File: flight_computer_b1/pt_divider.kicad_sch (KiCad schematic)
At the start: 4 parts

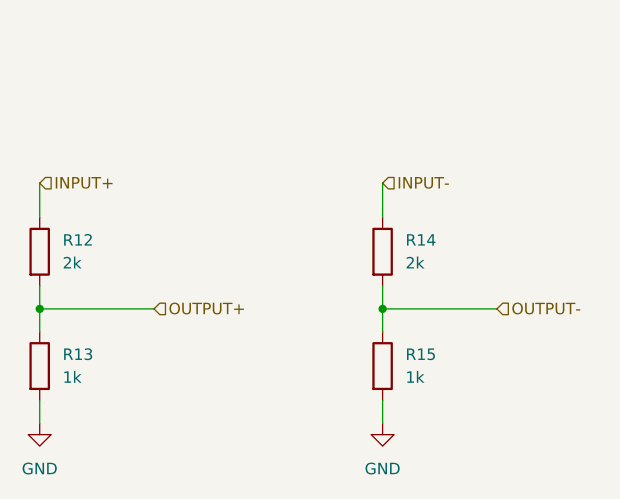
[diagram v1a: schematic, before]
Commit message: flight computer: added mux and voltage sense channels
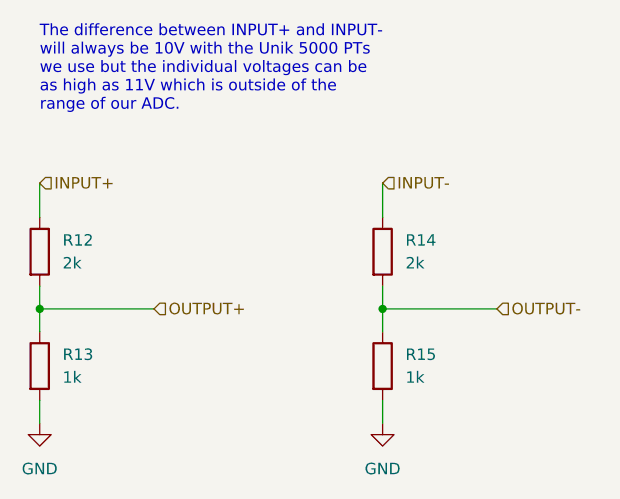
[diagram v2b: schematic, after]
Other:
- note added: "The difference between INPUT+ and INPUT- will always be 10V with the Unik 5000 PTs we use but the individual voltages can be as high as 11V which is outside of the range of our ADC."
- company: (none) -> Purdue Space Program Liquids

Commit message: flight computer: added pyro circuit and digikey part numbers
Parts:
- R12, R14: DIGIKEY PART N (none) -> 749-1706-1-ND
- R13, R15: DIGIKEY PART N (none) -> YAG1237CT-ND
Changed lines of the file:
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@@
+			)
+		)
+		(property "DIGIKEY PART N" "749-1706-1-ND"
+			(at 127 83.82 0)
+			(effects
+				(font
+					(size 1.27 1.27)
+				)
+				(hide yes)
 			)
 		)
@@
 			)
 		)
+		(property "DIGIKEY PART N" "749-1706-1-ND"
+			(at 165.1 83.82 0)
+			(effects
+				(font
+					(size 1.27 1.27)
+				)
+				(hide yes)
+			)
+		)
 		(pin "2"
 		)
@@
 			)
 		)
+		(property "DIGIKEY PART N" "YAG1237CT-ND"
+			(at 165.1 96.52 0)
+			(effects
+				(font
+					(size 1.27 1.27)
+				)
+				(hide yes)
+			)
+		)
 		(pin "2"
 		)
@@
 			(at 127 96.52 0)
 			(effects
+				(font
+					(size 1.27 1.27)
+				)
+				(hide yes)
+			)
+		)
+		(property "DIGIKEY PART N" "YAG1237CT-ND"
+			(at 127 96.52 0)
+			(effects

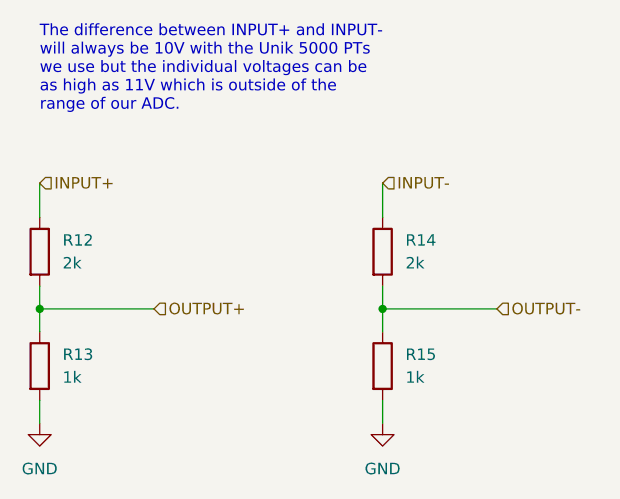
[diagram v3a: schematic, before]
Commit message: flight computer: routing updates
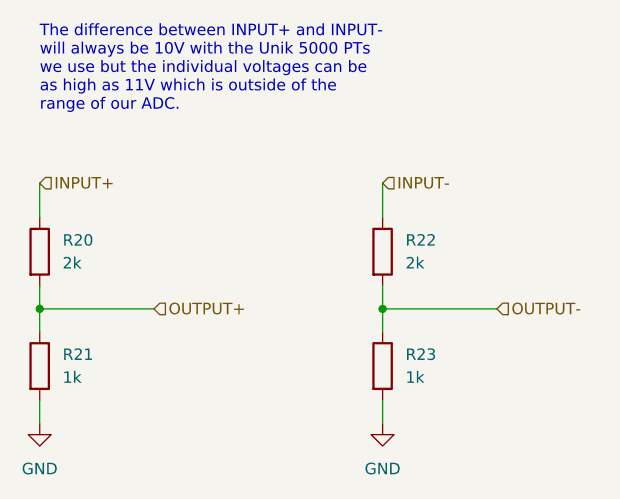
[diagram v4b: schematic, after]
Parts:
- renumbered R12 to R20, R13 to R21, R14 to R22, R15 to R23
